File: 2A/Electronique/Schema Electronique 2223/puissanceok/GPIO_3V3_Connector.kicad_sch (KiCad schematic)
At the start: 2 parts, among them J6 Conn_01x03

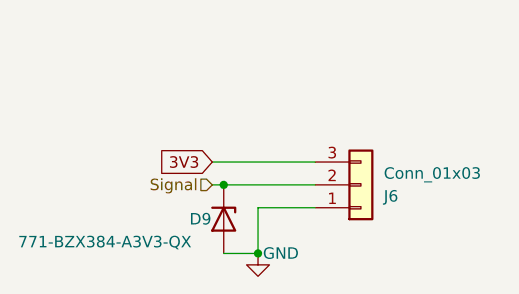
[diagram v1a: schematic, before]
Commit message: suppression diode et changement des feuille hiérarchique
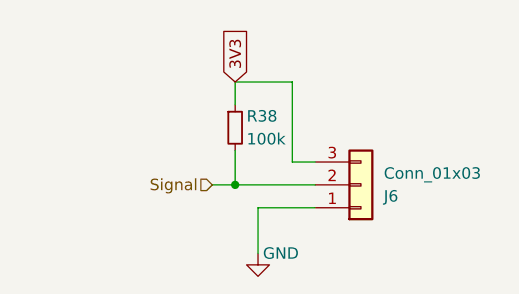
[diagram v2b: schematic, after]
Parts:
- removed D9: 771-BZX384-A3V3-QX, Diode_SMD:D_SOD-323, symbol Diode:BZX384xxxx
- added R38: 100k, Resistor_SMD:R_0402_1005Metric, symbol Device:R_Small
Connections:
- net 3V3: now also R38.1
- net Signal: now also R38.2
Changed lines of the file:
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@@
 (kicad_sch (version 20230121) (generator eeschema)
   (paper "A4")
-  (junction (at 138.43 107.95) (diameter 0) (color 0 0 0 0)
-  )
-  (junction (at 134.62 100.33) (diameter 0) (color 0 0 0 0)
+  (junction (at 135.89 100.33) (diameter 0) (color 0 0 0 0)
   )
   (wire (pts (xy 144.78 102.87) (xy 138.43 102.87))
@@
     (stroke (width 0) (type default))
   )
-  (wire (pts (xy 133.35 100.33) (xy 134.62 100.33))
+  (wire (pts (xy 135.89 88.9) (xy 135.89 91.44))
     (stroke (width 0) (type default))
   )
-  (wire (pts (xy 134.62 107.95) (xy 138.43 107.95))
+  (wire (pts (xy 142.24 97.79) (xy 144.78 97.79))
     (stroke (width 0) (type default))
   )
-  (wire (pts (xy 133.35 97.79) (xy 144.78 97.79))
+  (wire (pts (xy 135.89 100.33) (xy 144.78 100.33))
     (stroke (width 0) (type default))
   )
-  (wire (pts (xy 134.62 100.33) (xy 144.78 100.33))
+  (wire (pts (xy 142.24 88.9) (xy 142.24 97.79))
     (stroke (width 0) (type default))
   )
-  (global_label "3V3" (shape input) (at 133.35 97.79 180) (fields_autoplaced)
-    (effects (font (size 1.27 1.27)) (justify right))
-    (property "Intersheetrefs" "${INTERSHEET_REFS}" (at 126.8572 97.79 0)
-      (effects (font (size 1.27 1.27)) (justify right) hide)
+  (wire (pts (xy 135.89 96.52) (xy 135.89 100.33))
+    (stroke (width 0) (type default))
+  )
+  (wire (pts (xy 135.89 88.9) (xy 142.24 88.9))
+    (stroke (width 0) (type default))
+  )
+  (wire (pts (xy 133.35 100.33) (xy 135.89 100.33))
+    (stroke (width 0) (type default))
+  )
+  (global_label "3V3" (shape input) (at 135.89 88.9 90) (fields_autoplaced)
+    (effects (font (size 1.27 1.27)) (justify left))
+    (property "Intersheetrefs" "${INTERSHEET_REFS}" (at 135.89 82.4072 90)
+      (effects (font (size 1.27 1.27)) (justify left) hide)
     )
   )
@@
           (reference "#PWR039") (unit 1)
         )
-      )
-    )
-  )
-  (symbol (lib_id "Diode:BZX384xxxx") (at 134.62 104.14 270) (unit 1)
-    (in_bom yes) (on_board yes) (dnp no)
-    (property "Reference" "D9" (at 130.81 104.14 90)
-      (effects (font (size 1.27 1.27)) (justify left))
-    )
-    (property "Value" "771-BZX384-A3V3-QX" (at 111.76 106.68 90)
-      (effects (font (size 1.27 1.27)) (justify left))
-    )
-    (property "Footprint" "Diode_SMD:D_SOD-323" (at 130.175 104.14 0)
-      (effects (font (size 1.27 1.27)) hide)
-    )
-    (property "Datasheet" "https://www.mouser.fr/datasheet/2/916/BZX384_Q_SER-2721638.pdf" (at 134.62 104.14 0)
-      (effects (font (size 1.27 1.27)) hide)
-    )
-    (property "Mouser Part Number" "771-BZX384-A3V3-QX" (at 134.62 104.14 90)
-      (effects (font (size 1.27 1.27)) hide)
-    )
-    (pin "1")
-    (pin "2")
-    (instances
-      (project "puissanceok"
-        (path "/50648b18-b1a7-4d76-a5dd-1fad5f3e825e/1b14da9d-a013-4781-96ca-627f75997115"
-          (reference "D9") (unit 1)
+        (path "/50648b18-b1a7-4d76-a5dd-1fad5f3e825e/0bb23506-fa9f-4a6e-b1fd-c07f5de5ca14"
+          (reference "#PWR039") (unit 1)
         )
-        (path "/50648b18-b1a7-4d76-a5dd-1fad5f3e825e/9743065e-d1a0-48bf-a8c9-dead1a633504"
-          (reference "D9") (unit 1)
+        (path "/50648b18-b1a7-4d76-a5dd-1fad5f3e825e/68c40a5b-29d8-40fc-a6da-80692adf5f7e"
+          (reference "#PWR039") (unit 1)
         )
-        (path "/50648b18-b1a7-4d76-a5dd-1fad5f3e825e/3870049d-8cfc-48cf-b45e-10b2279efb87"
-          (reference "D9") (unit 1)
+        (path "/50648b18-b1a7-4d76-a5dd-1fad5f3e825e/2966dbe7-d86f-4e5a-a4e0-23b79617224c"
+          (reference "#PWR039") (unit 1)
         )
-        (path "/50648b18-b1a7-4d76-a5dd-1fad5f3e825e/50ee3374-811b-4a50-851a-2e3849343600"
-          (reference "D9") (unit 1)
+        (path "/50648b18-b1a7-4d76-a5dd-1fad5f3e825e/12c12d87-707a-4786-bdb3-8f38dcf02850"
+          (reference "#PWR039") (unit 1)
         )
       )
@@
           (reference "J6") (unit 1)
         )
+        (path "/50648b18-b1a7-4d76-a5dd-1fad5f3e825e/0bb23506-fa9f-4a6e-b1fd-c07f5de5ca14"
+          (reference "J6") (unit 1)
+        )
+        (path "/50648b18-b1a7-4d76-a5dd-1fad5f3e825e/68c40a5b-29d8-40fc-a6da-80692adf5f7e"
+          (reference "J6") (unit 1)
+        )
+        (path "/50648b18-b1a7-4d76-a5dd-1fad5f3e825e/2966dbe7-d86f-4e5a-a4e0-23b79617224c"
+          (reference "J6") (unit 1)
+        )
+        (path "/50648b18-b1a7-4d76-a5dd-1fad5f3e825e/12c12d87-707a-4786-bdb3-8f38dcf02850"
+          (reference "J6") (unit 1)
+        )
       )
+    )
+  )
+  (symbol (lib_id "Device:R_Small") (at 135.89 93.98 0) (unit 1)
+    (in_bom yes) (on_board yes) (dnp no)
+    (property "Reference" "R38" (at 137.16 92.71 0)
+      (effects (font (size 1.27 1.27)) (justify left))
+    )
+    (property "Value" "100k" (at 137.16 95.25 0)
+      (effects (font (size 1.27 1.27)) (justify left))
+    )
+    (property "Footprint" "Resistor_SMD:R_0402_1005Metric" (at 135.89 93.98 0)
+      (effects (font (size 1.27 1.27)) hide)
+    )
+    (property "Datasheet" "~" (at 135.89 93.98 0)
+      (effects (font (size 1.27 1.27)) hide)
+    )
+    (pin "1")
+    (pin "2")
+    (instances
+      (project "puissanceok"
+        (path "/50648b18-b1a7-4d76-a5dd-1fad5f3e825e/3870049d-8cfc-48cf-b45e-10b2279efb87"
+          (reference "R38") (unit 1)
+        )
+        (path "/50648b18-b1a7-4d76-a5dd-1fad5f3e825e/1b14da9d-a013-4781-96ca-627f75997115"
+          (reference "R39") (unit 1)
+        )
+        (path "/50648b18-b1a7-4d76-a5dd-1fad5f3e825e/9743065e-d1a0-48bf-a8c9-dead1a633504"
+          (reference "R40") (unit 1)
+        )
+        (path "/50648b18-b1a7-4d76-a5dd-1fad5f3e825e/50ee3374-811b-4a50-851a-2e3849343600"
+          (reference "R41") (unit 1)
+        )
+        (path "/50648b18-b1a7-4d76-a5dd-1fad5f3e825e/0bb23506-fa9f-4a6e-b1fd-c07f5de5ca14"
+          (reference "R42") (unit 1)
+        )
+        (path "/50648b18-b1a7-4d76-a5dd-1fad5f3e825e/68c40a5b-29d8-40fc-a6da-80692adf5f7e"
+          (reference "R43") (unit 1)
+        )
+        (path "/50648b18-b1a7-4d76-a5dd-1fad5f3e825e/2966dbe7-d86f-4e5a-a4e0-23b79617224c"
+          (reference "R44") (unit 1)
+        )
+        (path "/50648b18-b1a7-4d76-a5dd-1fad5f3e825e/12c12d87-707a-4786-bdb3-8f38dcf02850"
+          (reference "R45") (unit 1)
+        )
+      )

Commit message: update schematic
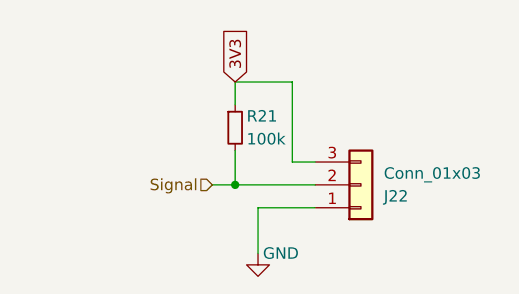
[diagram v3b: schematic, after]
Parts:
- renumbered J6 to J22, R38 to R21
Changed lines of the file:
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@@
   (symbol (lib_id "power:GND") (at 138.43 107.95 0) (unit 1)
     (in_bom yes) (on_board yes) (dnp no)
-    (property "Reference" "#PWR039" (at 138.43 114.3 0)
+    (property "Reference" "#PWR052" (at 138.43 114.3 0)
       (effects (font (size 1.27 1.27)) hide)
     )
@@
       (project "puissanceok"
         (path "/50648b18-b1a7-4d76-a5dd-1fad5f3e825e/1b14da9d-a013-4781-96ca-627f75997115"
-          (reference "#PWR039") (unit 1)
+          (reference "#PWR052") (unit 1)
         )
         (path "/50648b18-b1a7-4d76-a5dd-1fad5f3e825e/3870049d-8cfc-48cf-b45e-10b2279efb87"
-          (reference "#PWR039") (unit 1)
+          (reference "#PWR051") (unit 1)
         )
         (path "/50648b18-b1a7-4d76-a5dd-1fad5f3e825e/9743065e-d1a0-48bf-a8c9-dead1a633504"
-          (reference "#PWR039") (unit 1)
+          (reference "#PWR053") (unit 1)
         )
         (path "/50648b18-b1a7-4d76-a5dd-1fad5f3e825e/50ee3374-811b-4a50-851a-2e3849343600"
-          (reference "#PWR039") (unit 1)
+          (reference "#PWR054") (unit 1)
         )
         (path "/50648b18-b1a7-4d76-a5dd-1fad5f3e825e/0bb23506-fa9f-4a6e-b1fd-c07f5de5ca14"
-          (reference "#PWR039") (unit 1)
+          (reference "#PWR055") (unit 1)
         )
         (path "/50648b18-b1a7-4d76-a5dd-1fad5f3e825e/68c40a5b-29d8-40fc-a6da-80692adf5f7e"
-          (reference "#PWR039") (unit 1)
+          (reference "#PWR056") (unit 1)
         )
         (path "/50648b18-b1a7-4d76-a5dd-1fad5f3e825e/2966dbe7-d86f-4e5a-a4e0-23b79617224c"
-          (reference "#PWR039") (unit 1)
+          (reference "#PWR057") (unit 1)
         )
         (path "/50648b18-b1a7-4d76-a5dd-1fad5f3e825e/12c12d87-707a-4786-bdb3-8f38dcf02850"
-          (reference "#PWR039") (unit 1)
+          (reference "#PWR058") (unit 1)
         )
       )
@@
   (symbol (lib_id "Connector_Generic:Conn_01x03") (at 149.86 100.33 0) (mirror x) (unit 1)
     (in_bom yes) (on_board yes) (dnp no)
-    (property "Reference" "J6" (at 152.4 101.6 0)
+    (property "Reference" "J22" (at 152.4 101.6 0)
       (effects (font (size 1.27 1.27)) (justify left))
     )
@@
       (project "puissanceok"
         (path "/50648b18-b1a7-4d76-a5dd-1fad5f3e825e/1b14da9d-a013-4781-96ca-627f75997115"
-          (reference "J6") (unit 1)
+          (reference "J22") (unit 1)
         )
         (path "/50648b18-b1a7-4d76-a5dd-1fad5f3e825e/9743065e-d1a0-48bf-a8c9-dead1a633504"
-          (reference "J6") (unit 1)
+          (reference "J23") (unit 1)
         )
         (path "/50648b18-b1a7-4d76-a5dd-1fad5f3e825e/3870049d-8cfc-48cf-b45e-10b2279efb87"
-          (reference "J6") (unit 1)
+          (reference "J21") (unit 1)
         )
         (path "/50648b18-b1a7-4d76-a5dd-1fad5f3e825e/50ee3374-811b-4a50-851a-2e3849343600"
-          (reference "J6") (unit 1)
+          (reference "J24") (unit 1)
         )
         (path "/50648b18-b1a7-4d76-a5dd-1fad5f3e825e/0bb23506-fa9f-4a6e-b1fd-c07f5de5ca14"
-          (reference "J6") (unit 1)
+          (reference "J25") (unit 1)
         )
         (path "/50648b18-b1a7-4d76-a5dd-1fad5f3e825e/68c40a5b-29d8-40fc-a6da-80692adf5f7e"
-          (reference "J6") (unit 1)
+          (reference "J26") (unit 1)
         )
         (path "/50648b18-b1a7-4d76-a5dd-1fad5f3e825e/2966dbe7-d86f-4e5a-a4e0-23b79617224c"
-          (reference "J6") (unit 1)
+          (reference "J27") (unit 1)
         )
         (path "/50648b18-b1a7-4d76-a5dd-1fad5f3e825e/12c12d87-707a-4786-bdb3-8f38dcf02850"
-          (reference "J6") (unit 1)
+          (reference "J28") (unit 1)
         )
       )
@@
   (symbol (lib_id "Device:R_Small") (at 135.89 93.98 0) (unit 1)
     (in_bom yes) (on_board yes) (dnp no)
-    (property "Reference" "R38" (at 137.16 92.71 0)
+    (property "Reference" "R21" (at 137.16 92.71 0)
       (effects (font (size 1.27 1.27)) (justify left))
     )
@@
       (project "puissanceok"
         (path "/50648b18-b1a7-4d76-a5dd-1fad5f3e825e/3870049d-8cfc-48cf-b45e-10b2279efb87"
-          (reference "R38") (unit 1)
+          (reference "R21") (unit 1)
         )
         (path "/50648b18-b1a7-4d76-a5dd-1fad5f3e825e/1b14da9d-a013-4781-96ca-627f75997115"
-          (reference "R39") (unit 1)
+          (reference "R22") (unit 1)
         )
         (path "/50648b18-b1a7-4d76-a5dd-1fad5f3e825e/9743065e-d1a0-48bf-a8c9-dead1a633504"
-          (reference "R40") (unit 1)
+          (reference "R23") (unit 1)
         )
         (path "/50648b18-b1a7-4d76-a5dd-1fad5f3e825e/50ee3374-811b-4a50-851a-2e3849343600"
-          (reference "R41") (unit 1)
+          (reference "R24") (unit 1)
         )
         (path "/50648b18-b1a7-4d76-a5dd-1fad5f3e825e/0bb23506-fa9f-4a6e-b1fd-c07f5de5ca14"
-          (reference "R42") (unit 1)
+          (reference "R25") (unit 1)
         )
         (path "/50648b18-b1a7-4d76-a5dd-1fad5f3e825e/68c40a5b-29d8-40fc-a6da-80692adf5f7e"
-          (reference "R43") (unit 1)
+          (reference "R26") (unit 1)
         )
         (path "/50648b18-b1a7-4d76-a5dd-1fad5f3e825e/2966dbe7-d86f-4e5a-a4e0-23b79617224c"
-          (reference "R44") (unit 1)
+          (reference "R27") (unit 1)
         )
         (path "/50648b18-b1a7-4d76-a5dd-1fad5f3e825e/12c12d87-707a-4786-bdb3-8f38dcf02850"
-          (reference "R45") (unit 1)
+          (reference "R28") (unit 1)
         )
       )

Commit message: debut assignation empreintes
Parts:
- R21: footprint Resistor_SMD:R_0402_1005Metric -> Resistor_SMD:R_0603_1608Metric_Pad0.98x0.95mm_HandSolder
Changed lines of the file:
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@@
       (effects (font (size 1.27 1.27)) (justify left))
     )
-    (property "Footprint" "Resistor_SMD:R_0402_1005Metric" (at 135.89 93.98 0)
+    (property "Footprint" "Resistor_SMD:R_0603_1608Metric_Pad0.98x0.95mm_HandSolder" (at 135.89 93.98 0)
       (effects (font (size 1.27 1.27)) hide)
     )
